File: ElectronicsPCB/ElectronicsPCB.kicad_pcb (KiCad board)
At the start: 4 copper layers, 16 parts

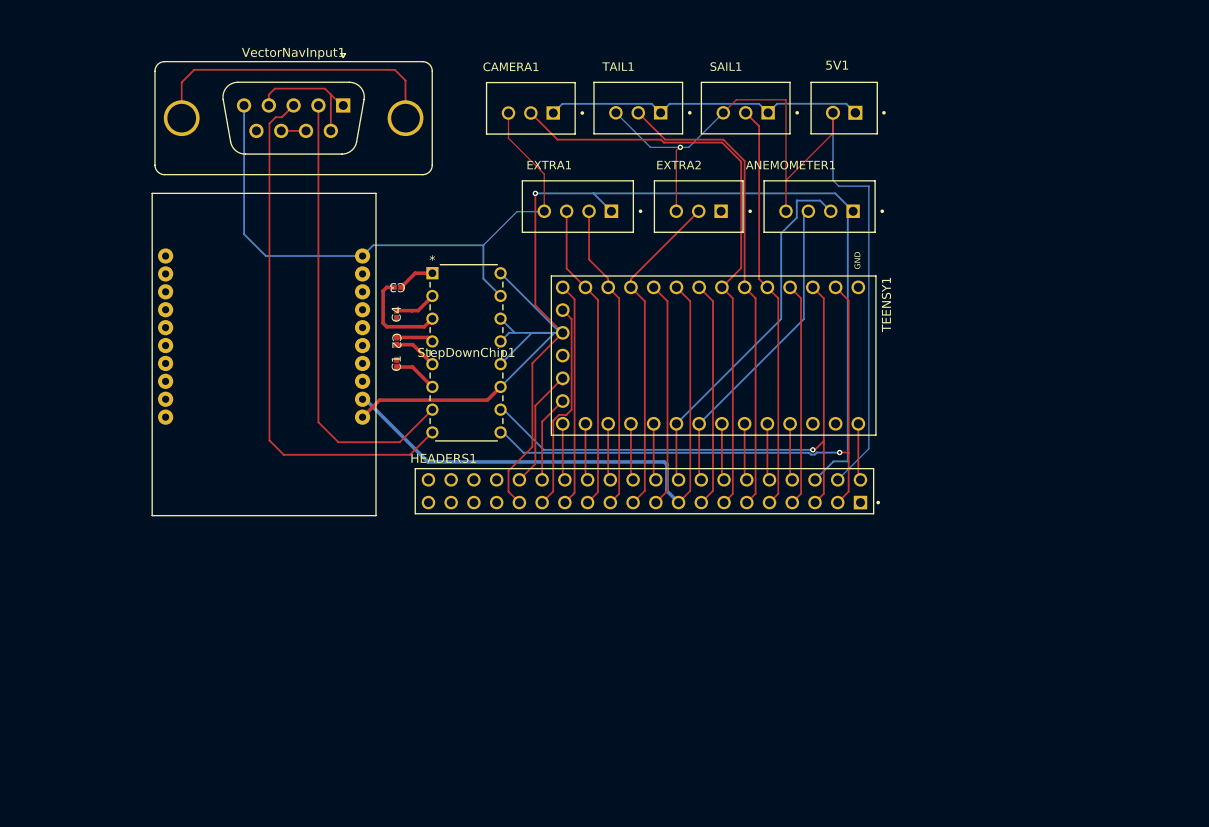
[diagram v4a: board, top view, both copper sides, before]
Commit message: added mounting holes
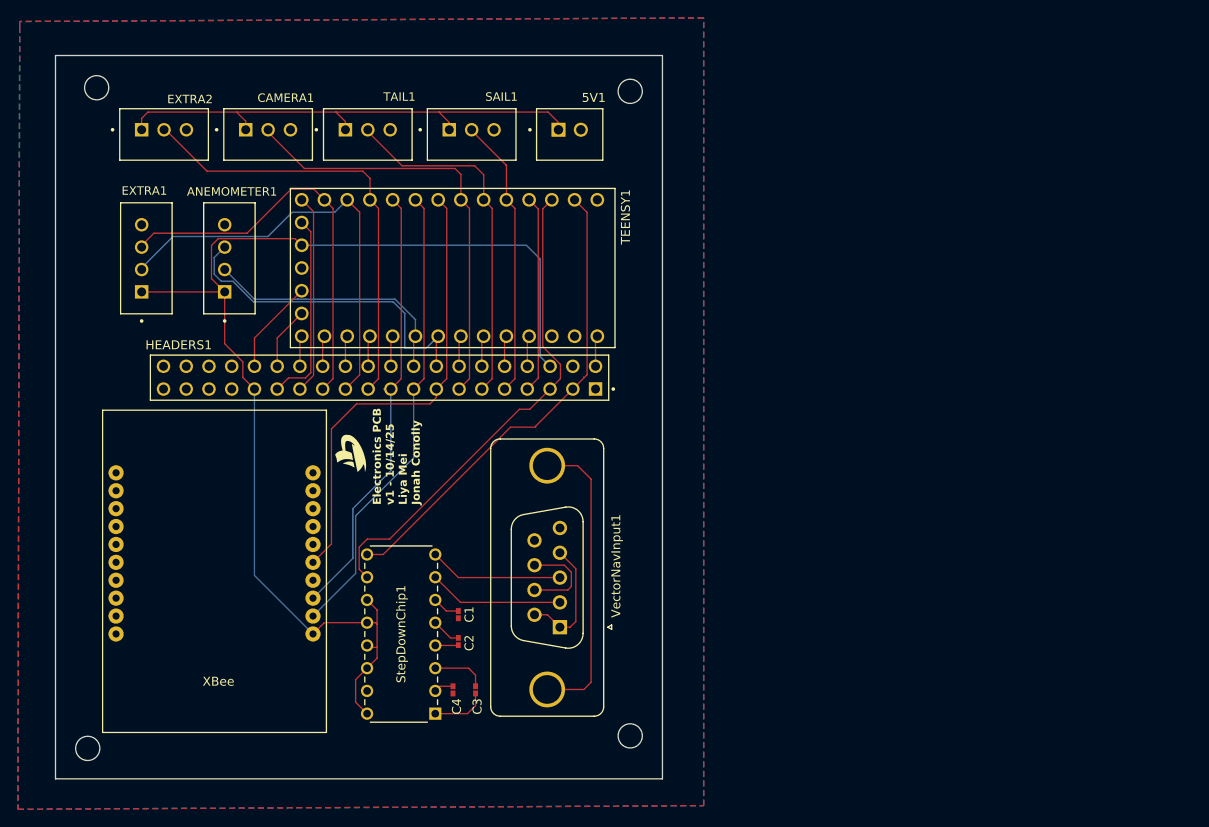
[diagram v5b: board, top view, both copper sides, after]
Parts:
- added G***: LOGO, LOGO, F.Cu at (130.4, 97.0)
- added H1: MountingHole, MountingHole:MountingHole_2.7mm, F.Cu at (102.0, 56.2)
- added H2: MountingHole, MountingHole:MountingHole_2.7mm, F.Cu at (161.6, 56.6)
- added H3: MountingHole, MountingHole:MountingHole_2.7mm, F.Cu at (101.0, 130.0)
- added H4: MountingHole, MountingHole:MountingHole_2.7mm, F.Cu at (161.6, 128.6)
- moved ANEMOMETER1 66.2 mm to (116.8, 75.3), turned to -90 degrees
- moved VectorNavInput1 63.1 mm to (153.7, 116.5), turned to -90 degrees
- moved EXTRA2 60.3 mm to (109.5, 61.4), turned to 180 degrees
- moved StepDownChip1 49.2 mm to (139.8, 126.1), turned to 180 degrees
- moved EXTRA1 48.5 mm to (107.5, 75.3), turned to -90 degrees
- moved C3 45.8 mm to (144.3, 123.5), turned to 90 degrees
- moved C4 42.4 mm to (141.8, 123.5)
- moved C2 34.3 mm to (142.4, 118.1), turned to 90 degrees
- moved HEADERS1 32.2 mm to (133.6, 88.6)
- moved 5V1 30.8 mm to (154.8, 61.4), turned to 180 degrees
- moved SAIL1 30.8 mm to (143.9, 61.4), turned to 180 degrees
- moved TEENSY1 30.8 mm to (141.4, 76.3)
- moved TAIL1 30.4 mm to (132.3, 61.4), turned to 180 degrees
- moved CAMERA1 29.5 mm to (121.2, 61.4), turned to 180 degrees
- moved C1 28.9 mm to (142.4, 115.1), turned to -90 degrees
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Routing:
- net GND: track 170.1 -> 0.22 mm, vias 1 -> 0
- net VectorNavTX: track 58.8 -> 15.0 mm
- net VectorNavRX: track 50.6 -> 15.1 mm
- net +3.3V: track 165.1 -> 132.2 mm, vias 1 -> 0
- net XBeeRESET: track 25.2 -> 51.9 mm
- net XBeeRX: track 25.2 -> 49.8 mm
- net +5V: track 36.3 -> 57.1 mm
- net Camera: track 65.6 -> 48.3 mm
- net XBeeTX: track 67.0 -> 52.0 mm
- net Sail: track 45.5 -> 31.1 mm
- net Extra40: track 34.3 -> 48.5 mm
- net Tail: track 53.2 -> 39.1 mm
- net Extra3: track 36.9 -> 49.1 mm
- net WindData0: track 41.2 -> 29.0 mm
- net TeensyRX: track 65.2 -> 53.1 mm, vias 1 -> 0
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- added copper zone on B.Cu, net GND
- added copper zone on F.Cu, net GND
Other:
- board outline added: 67.8 x 80.8 mm
- board text added: "Electronics PCB v1 - 10/14/25 Liya Mei Jonah Conolly"

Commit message: fixed DRC issues and added clipart
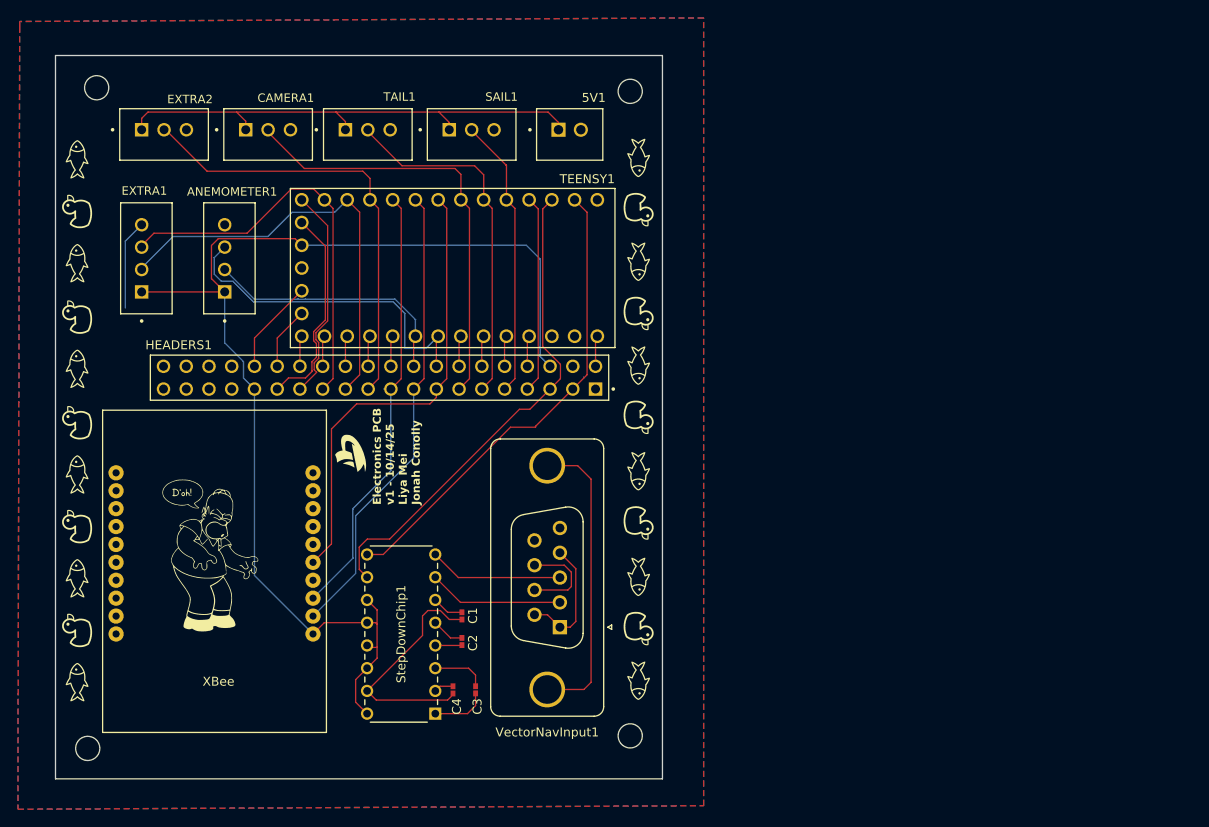
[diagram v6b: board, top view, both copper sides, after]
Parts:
- added G***: LOGO, LOGO, F.Cu at (162.5, 110.8)
- added G***: LOGO, LOGO, F.Cu at (99.8, 116.8)
- added G***: LOGO, LOGO, F.Cu at (162.6, 104.8)
- added G***: LOGO, LOGO, F.Cu at (162.6, 69.8)
- added G***: LOGO, LOGO, F.Cu at (162.5, 87.2)
- added G***: LOGO, LOGO, F.Cu at (114.8, 108.4)
- added G***: LOGO, LOGO, F.Cu at (99.8, 87.6)
- added G***: LOGO, LOGO, F.Cu at (162.5, 99.0)
- added G***: LOGO, LOGO, F.Cu at (162.6, 81.4)
- added G***: LOGO, LOGO, F.Cu at (99.8, 122.6)
- added G***: LOGO, LOGO, F.Cu at (99.8, 81.8)
- added G***: LOGO, LOGO, F.Cu at (99.8, 111.0)
- added G***: LOGO, LOGO, F.Cu at (99.8, 64.2)
- added G***: LOGO, LOGO, F.Cu at (99.8, 99.4)
- added G***: LOGO, LOGO, F.Cu at (162.5, 75.6)
- added G***: LOGO, LOGO, F.Cu at (162.6, 116.6)
- added G***: LOGO, LOGO, F.Cu at (99.8, 75.8)
- added G***: LOGO, LOGO, F.Cu at (162.6, 93.0)
- added G***: LOGO, LOGO, F.Cu at (99.8, 105.2)
- added G***: LOGO, LOGO, F.Cu at (162.5, 122.4)
- added G***: LOGO, LOGO, F.Cu at (99.8, 70.0)
- added G***: LOGO, LOGO, F.Cu at (99.8, 93.6)
- added G***: LOGO, LOGO, F.Cu at (162.5, 64.0)
- moved C1 0.42 mm to (142.8, 115.2)
- moved C2 0.40 mm to (142.8, 118.1)
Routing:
- net GND: track 0.22 -> 37.2 mm
- net 12: track 22.3 -> 24.1 mm
- net VBAT: track 21.7 -> 23.3 mm

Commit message: updated text on control board
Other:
- board text added: "Control PCB Fall 2025 Liya Mei Jonah Conolly"
- board text removed: "Electronics PCB v1 - 10/14/25 Liya Mei Jonah Conolly"
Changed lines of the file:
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@@
 			(fill yes)
 			(layer "F.SilkS")
-			(net 4745664)
 		)
 		(fp_poly
@@
 			(fill yes)
 			(layer "F.SilkS")
-			(net 4745664)
 		)
 		(embedded_fonts no)
@@
 			(fill yes)
 			(layer "F.SilkS")
-			(net 4745664)
 		)
 		(fp_poly
@@
 			(fill yes)
 			(layer "F.SilkS")
-			(net 4745664)
 		)
 		(embedded_fonts no)
@@
 		(layer "Edge.Cuts")
 	)
-	(gr_text "Electronics PCB \nv1 - 10/14/25\nLiya Mei\nJonah Conolly"
+	(gr_text "Control PCB\nFall 2025\nLiya Mei\nJonah Conolly"
 		(at 138.2 102.8 90)
 		(layer "F.SilkS")

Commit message: fixed teensy power on electronics PCB
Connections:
- HEADERS1 pad 2: TeensyVIN -> +5V
- TEENSY1 pad VIN: TeensyVIN -> +5V
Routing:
- net +5V: track 57.1 -> 86.3 mm
- net TeensyVIN: track 3.52 -> 0.00 mm
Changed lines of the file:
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@@
 	(net 31 "ON_OFF")
 	(net 32 "unconnected-(HEADERS1-Pad38)")
-	(net 33 "TeensyVIN")
+	(net 33 "unconnected-(VectorNavInput1-PAD-Pad0)_1")
 	(net 34 "20")
 	(net 35 "VBAT")
@@
 			)
 		)
+		(property ki_fp_filters "DSUB*Socket*")
+		(sheetname "/")
+		(sheetfile "ElectronicsPCB.kicad_sch")
 		(attr through_hole)
 		(fp_line
@@
 			(layers "*.Cu" "*.Mask")
 			(remove_unused_layers no)
-			(net 52 "unconnected-(VectorNavInput1-PAD-Pad0)")
+			(net 33 "unconnected-(VectorNavInput1-PAD-Pad0)_1")
 			(pinfunction "PAD")
-			(pintype "passive")
+			(pintype "passive+no_connect")
 		)
 		(pad "0" thru_hole circle
@@
 			(net 52 "unconnected-(VectorNavInput1-PAD-Pad0)")
 			(pinfunction "PAD")
-			(pintype "passive")
+			(pintype "passive+no_connect")
 		)
 		(pad "1" thru_hole rect
@@
 			(net 54 "unconnected-(VectorNavInput1-Pad9)")
 			(pinfunction "9")
-			(pintype "passive")
+			(pintype "passive+no_connect")
 		)
 		(embedded_fonts no)
@@
 			)
 		)
+		(property ki_fp_filters "C_*")
+		(sheetname "/")
+		(sheetfile "ElectronicsPCB.kicad_sch")
 		(attr smd)
 		(fp_line
@@
 			)
 		)
+		(sheetname "/")
+		(sheetfile "ElectronicsPCB.kicad_sch")
 		(attr through_hole)
 		(fp_line
@@
 			)
 		)
+		(sheetname "/")
+		(sheetfile "ElectronicsPCB.kicad_sch")
 		(attr through_hole)
 		(fp_line
@@
 			)
 		)
+		(sheetname "/")
+		(sheetfile "ElectronicsPCB.kicad_sch")
 		(attr through_hole)
 		(fp_line
@@
 			)
 		)
+		(sheetname "/")
+		(sheetfile "ElectronicsPCB.kicad_sch")
 		(attr through_hole)
 		(fp_line
@@
 			)
 		)
+		(property ki_fp_filters "C_*")
+		(sheetname "/")
+		(sheetfile "ElectronicsPCB.kicad_sch")
 		(attr smd)
 		(fp_line
@@
 			)
 		)
+		(sheetname "/")
+		(sheetfile "ElectronicsPCB.kicad_sch")
 		(attr through_hole)
 		(fp_line
@@
 			(layers "*.Cu" "*.Mask")
 			(remove_unused_layers no)
-			(net 33 "TeensyVIN")
+			(net 11 "+5V")
 			(pinfunction "2")
 			(pintype "passive")
@@
 			)
 		)
+		(sheetname "/")
+		(sheetfile "ElectronicsPCB.kicad_sch")
 		(attr through_hole)
 		(fp_line
@@
 			(layers "*.Cu" "*.Mask")
 			(remove_unused_layers no)
-			(net 33 "TeensyVIN")
+			(net 11 "+5V")
 			(pinfunction "VIN")
 			(pintype "power_in")
@@
 			)
 		)
+		(property ki_fp_filters "21-0043_P16+3_MXM")
+		(sheetname "/")
+		(sheetfile "ElectronicsPCB.kicad_sch")
 		(attr through_hole)
 		(fp_line
@@
 			)
 		)
+		(property ki_fp_filters "C_*")
+		(sheetname "/")
+		(sheetfile "ElectronicsPCB.kicad_sch")
 		(attr smd)
 		(fp_line
@@
 			)
 		)
+		(sheetname "/")
+		(sheetfile "ElectronicsPCB.kicad_sch")
 		(attr through_hole)
 		(fp_line
@@
 			)
 		)
+		(property ki_fp_filters "CONN_B4B-XH-A_JST")
+		(sheetname "/")
+		(sheetfile "ElectronicsPCB.kicad_sch")
 		(attr through_hole)
 		(fp_line
@@
 			)
 		)
+		(property ki_fp_filters "CONN_B4B-XH-A_JST")
+		(sheetname "/")
+		(sheetfile "ElectronicsPCB.kicad_sch")
 		(attr through_hole)
 		(fp_line
@@
 			)
 		)
+		(sheetname "/")
+		(sheetfile "ElectronicsPCB.kicad_sch")
 		(attr through_hole)
 		(fp_line
@@
 			)
 		)
+		(property ki_fp_filters "C_*")
+		(sheetname "/")
+		(sheetfile "ElectronicsPCB.kicad_sch")
 		(attr smd)
 		(fp_line
@@
 	)
 	(segment
+		(start 157.785 83.95875)
+		(end 157.725 84.01875)
+		(width 0.127)
+		(layer "F.Cu")
+		(net 11)
+	)
+	(segment
 		(start 107.725 58.91875)
 		(end 117.625 58.91875)
@@
 	)
 	(segment
+		(start 157.925 83.95875)
+		(end 157.785 83.95875)
+		(width 0.127)
+		(layer "F.Cu")
+		(net 11)
+	)
+	(segment
 		(start 140.225 58.91875)
 		(end 141.3875 60.08125)
@@
 	)
 	(segment
+		(start 158.88375 83)
+		(end 158.88375 66.19)
+		(width 0.127)
+		(layer "F.Cu")
+		(net 11)
+	)
+	(segment
 		(start 128.725 58.91875)
 		(end 129.7875 59.98125)
@@
 	)
 	(segment
+		(start 157.725 84.01875)
+		(end 157.725 87.31875)
+		(width 0.127)
+		(layer "F.Cu")
+		(net 11)
+	)
+	(segment
 		(start 140.225 58.91875)
 		(end 152.425 58.91875)
@@
 	)
 	(segment
+		(start 157.925 83.95875)
+		(end 158.88375 83)
+		(width 0.127)
+		(layer "F.Cu")
+		(net 11)
+	)
+	(segment
+		(start 158.88375 66.19)
+		(end 153.5875 60.89375)
+		(width 0.127)
+		(layer "F.Cu")
+		(net 11)
+	)
+	(segment
 		(start 128.725 58.91875)
 		(end 140.225 58.91875)
@@
 	)
 	(segment
-		(start 157.785 83.95875)
-		(end 157.725 84.01875)
-		(width 0.127)
-		(layer "F.Cu")
-		(net 33)
-	)
-	(segment
-		(start 157.925 83.95875)
-		(end 157.785 83.95875)
-		(width 0.127)
-		(layer "F.Cu")
-		(net 33)
-	)
-	(segment
-		(start 157.725 84.01875)
-		(end 157.725 87.31875)
-		(width 0.127)
-		(layer "F.Cu")
-		(net 33)
-	)
-	(segment
